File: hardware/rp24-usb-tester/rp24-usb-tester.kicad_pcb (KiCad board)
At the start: 2 copper layers, 50 x 25 mm, 40 parts, among them J1 SPEAKER, J2 POWER, J3 EXT_CAP, J4 505070-2422, J5 RAILS, J6 AUX, J7 MOTOR, P1 USB_C_Receptacle_USB2.0_16P, Q1 SS8050, Q2 SS8050, Q3 SS8050, Q4 SS8050, Q5 SS8050, U1 MT2492

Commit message: chore: include 3d components
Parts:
- C1, C3: footprint Capacitor_SMD:C_0805_2012Metric -> rp24-usb-tester:C_0805_2012Metric
- C2: footprint Capacitor_SMD:C_0402_1005Metric -> rp24-usb-tester:C_0402_1005Metric
- D1, D10, D11, D12, D14, D2, D3, D4, D5, D6, D7, D8, D9: footprint LED_SMD:LED_0603_1608Metric -> rp24-usb-tester:LED_0603_1608Metric
- D13: footprint Diode_SMD:D_SMA -> rp24-usb-tester:D_SMA
- J1, J3, J5, J7: footprint Connector_PinHeader_2.54mm:PinHeader_1x02_P2.54mm_Vertical -> rp24-usb-tester:PinHeader_1x02_P2.54mm_Vertical
- J2: footprint Connector_PinHeader_2.54mm:PinHeader_1x04_P2.54mm_Vertical -> rp24-usb-tester:PinHeader_1x04_P2.54mm_Vertical
- J6: footprint Connector_PinHeader_2.54mm:PinHeader_1x05_P2.54mm_Vertical -> rp24-usb-tester:PinHeader_1x05_P2.54mm_Vertical
- P1: footprint Connector_USB:USB_C_Receptacle_GCT_USB4105-xx-A_16P_TopMnt_Horizontal -> rp24-usb-tester:USB_C_Receptacle_GCT_USB4105-xx-A_16P_TopMnt_Horizontal
- Q1, Q2, Q3, Q4, Q5: footprint Package_TO_SOT_SMD:SOT-23 -> rp24-usb-tester:SOT-23
- R1, R2, R5: footprint Resistor_SMD:R_0402_1005Metric -> rp24-usb-tester:R_0402_1005Metric
- R3, R4: footprint Resistor_SMD:R_0603_1608Metric -> rp24-usb-tester:R_0603_1608Metric
- RN1, RN2, RN3: footprint Resistor_SMD:R_Array_Concave_4x0402 -> rp24-usb-tester:R_Array_Concave_4x0402
- U1: footprint Package_TO_SOT_SMD:SOT-23-6 -> rp24-usb-tester:SOT-23-6

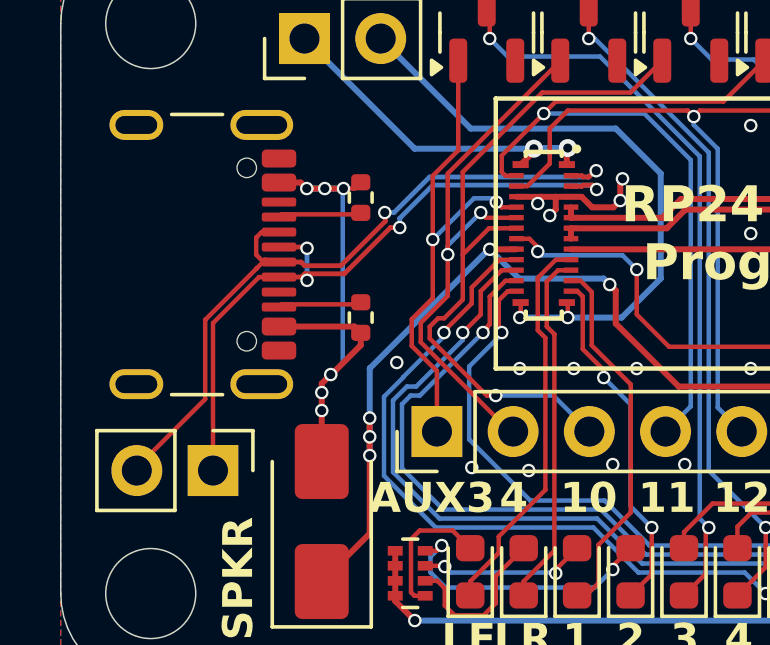
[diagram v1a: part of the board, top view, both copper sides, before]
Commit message: fix: 5.1k resistors go to gnd
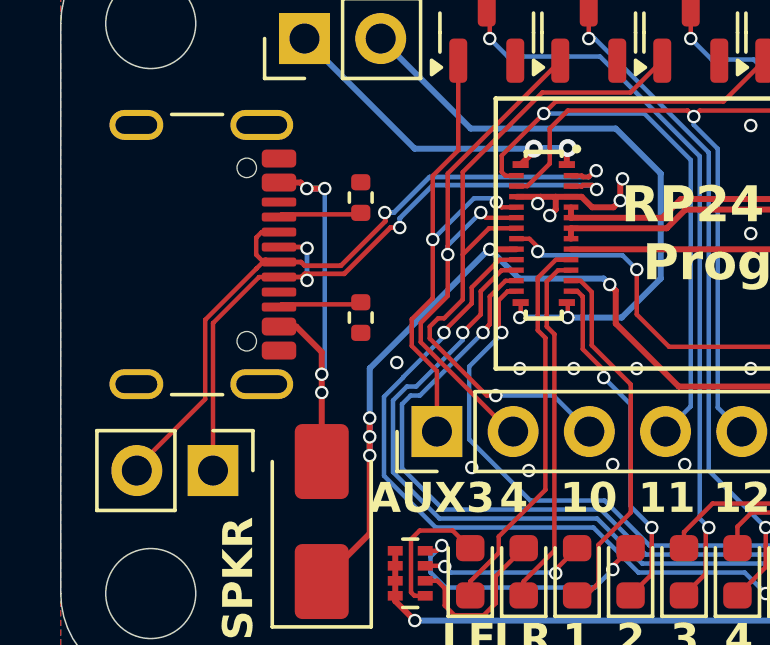
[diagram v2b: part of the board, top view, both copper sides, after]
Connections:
- R1 pad 2: VBUS -> GND
- R2 pad 1: VBUS -> GND
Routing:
- net VBUS: track 19.5 -> 14.5 mm, vias 6 -> 4
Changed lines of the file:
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@@
 			(psa4output no)
 			(plot_black_and_white yes)
-			(plotinvisibletext no)
 			(sketchpadsonfab no)
 			(plotpadnumbers no)
@@
 			)
 		)
-		(property "Datasheet" ""
+		(property "Datasheet" "~"
 			(at 0 0 90)
 			(unlocked yes)
@@
 			)
 		)
-		(property "Datasheet" ""
+		(property "Datasheet" "~"
 			(at 0 0 90)
 			(unlocked yes)
@@
 			)
 		)
-		(property "Datasheet" ""
+		(property "Datasheet" "~"
 			(at 0 0 90)
 			(unlocked yes)
@@
 			)
 		)
-		(property "Datasheet" ""
+		(property "Datasheet" "~"
 			(at 0 0 90)
 			(unlocked yes)
@@
 			)
 		)
-		(property "Datasheet" ""
+		(property "Datasheet" "~"
 			(at 0 0 90)
 			(unlocked yes)
@@
 			)
 		)
-		(property "Datasheet" ""
+		(property "Datasheet" "~"
 			(at 0 0 0)
 			(unlocked yes)
@@
 			)
 		)
-		(property "Datasheet" ""
+		(property "Datasheet" "~"
 			(at 0 0 0)
 			(unlocked yes)
@@
 			)
 		)
-		(property "Datasheet" ""
+		(property "Datasheet" "~"
 			(at 0 0 90)
 			(unlocked yes)
@@
 			)
 		)
-		(property "Datasheet" ""
+		(property "Datasheet" "~"
 			(at 0 0 90)
 			(unlocked yes)
@@
 			)
 		)
-		(property "Datasheet" ""
+		(property "Datasheet" "~"
 			(at 0 0 90)
 			(unlocked yes)
@@
 			(layers "F.Cu" "F.Mask" "F.Paste")
 			(roundrect_rratio 0.25)
-			(net 47 "VBUS")
+			(net 26 "GND")
 			(pintype "passive")
 		)
@@
 			)
 		)
-		(property "Datasheet" ""
+		(property "Datasheet" "~"
 			(at 0 0 90)
 			(unlocked yes)
@@
 			)
 		)
-		(property "Datasheet" ""
+		(property "Datasheet" "~"
 			(at 0 0 90)
 			(unlocked yes)
@@
 			)
 		)
-		(property "Datasheet" ""
+		(property "Datasheet" "~"
 			(at 0 0 90)
 			(unlocked yes)
@@
 			)
 		)
-		(property "Datasheet" ""
+		(property "Datasheet" "~"
 			(at 0 0 0)
 			(unlocked yes)
@@
 			)
 		)
-		(property "Datasheet" ""
+		(property "Datasheet" "~"
 			(at 0 0 90)
 			(unlocked yes)
@@
 			(layers "F.Cu" "F.Mask" "F.Paste")
 			(roundrect_rratio 0.25)
-			(net 47 "VBUS")
+			(net 26 "GND")
 			(pintype "passive")
 		)
@@
 			)
 		)
-		(property "Datasheet" ""
+		(property "Datasheet" "~"
 			(at 0 0 270)
 			(unlocked yes)
@@
 			)
 		)
-		(property "Datasheet" ""
+		(property "Datasheet" "~"
 			(at 0 0 180)
 			(unlocked yes)
@@
 			)
 		)
-		(property "Datasheet" ""
+		(property "Datasheet" "~"
 			(at 0 0 90)
 			(unlocked yes)
@@
 			)
 		)
-		(property "Datasheet" ""
+		(property "Datasheet" "~"
 			(at 0 0 90)
 			(unlocked yes)
@@
 			)
 		)
-		(property "Datasheet" ""
+		(property "Datasheet" "~"
 			(at 0 0 90)
 			(unlocked yes)
@@
 			)
 		)
-		(property "Datasheet" ""
+		(property "Datasheet" "~"
 			(at 0 0 0)
 			(layer "F.Fab")
@@
 			)
 		)
-		(property "Datasheet" ""
+		(property "Datasheet" "~"
 			(at 0 0 90)
 			(unlocked yes)
@@
 			)
 		)
-		(property "Datasheet" ""
+		(property "Datasheet" "~"
 			(at 0 0 90)
 			(unlocked yes)
@@
 			)
 		)
-		(property "Datasheet" ""
+		(property "Datasheet" "~"
 			(at 0 0 90)
 			(unlocked yes)
@@
 			)
 		)
-		(property "Datasheet" ""
+		(property "Datasheet" "~"
 			(at 0 0 270)
 			(unlocked yes)
@@
 			)
 		)
-		(property "Datasheet" ""
+		(property "Datasheet" "~"
 			(at 0 0 270)
 			(unlocked yes)
@@
 			)
 		)
-		(property "Datasheet" ""
+		(property "Datasheet" "~"
 			(at 0 0 90)
 			(unlocked yes)
@@
 			)
 		)
-		(property "Datasheet" ""
+		(property "Datasheet" "~"
 			(at 0 0 0)
 			(unlocked yes)
@@
 			)
 		)
-		(property "Datasheet" ""
+		(property "Datasheet" "~"
 			(at 0 0 90)
 			(unlocked yes)
@@
 			)
 		)
-		(property "Datasheet" ""
+		(property "Datasheet" "~"
 			(at 0 0 90)
 			(unlocked yes)
@@
 			)
 		)
-		(property "Datasheet" ""
+		(property "Datasheet" "~"
 			(at 0 0 90)
 			(unlocked yes)
@@
 	)
 	(segment
-		(start 134.3 108)
-		(end 133.7 108)
+		(start 134.2 113.450001)
+		(end 134.2 114.19)
 		(width 0.2)
 		(layer "F.Cu")
@@
 	)
 	(segment
-		(start 134.925003 108)
-		(end 134.3 108)
+		(start 134.3 108)
+		(end 133.7 108)
 		(width 0.2)
 		(layer "F.Cu")
@@
 	)
 	(segment
-		(start 134.5 114.2)
-		(end 134.525 114.2)
-		(width 0.4)
-		(layer "F.Cu")
-		(net 47)
-	)
-	(segment
-		(start 135.5 113.225)
-		(end 134.525 114.2)
+		(start 132.775 112.6)
+		(end 133.349999 112.6)
 		(width 0.2)
 		(layer "F.Cu")
@@
 	)
 	(segment
-		(start 134.5 114.2)
-		(end 134.2 114.5)
-		(width 0.2)
-		(layer "F.Cu")
-		(net 47)
-	)
-	(segment
 		(start 133.5 107.8)
 		(end 133.7 108)
@@
 	)
 	(segment
-		(start 135.29 112.6)
-		(end 135.5 112.81)
-		(width 0.2)
-		(layer "F.Cu")
-		(net 47)
-	)
-	(segment
-		(start 135.5 112.81)
-		(end 135.5 113.225)
-		(width 0.2)
-		(layer "F.Cu")
-		(net 47)
-	)
-	(segment
-		(start 135.29 108)
-		(end 135.5 107.79)
-		(width 0.15)
-		(layer "F.Cu")
-		(net 47)
-	)
-	(segment
-		(start 134.2 114.5)
+		(start 134.2 114.19)
 		(end 134.2 117.1)
 		(width 0.2)
@@
 	)
 	(segment
-		(start 134.925003 108)
-		(end 135.29 108)
-		(width 0.15)
+		(start 133.349999 112.6)
+		(end 134.2 113.450001)
+		(width 0.2)
 		(layer "F.Cu")
 		(net 47)
 	)
 	(segment
-		(start 132.775 112.6)
-		(end 135.29 112.6)
-		(width 0.2)
+		(start 134.2 114.19)
+		(end 134.21 114.2)
+		(width 0.4)
 		(layer "F.Cu")
 		(net 47)
 	)
 	(via
-		(at 134.5 114.2)
-		(size 0.45)
-		(drill 0.3)
-		(layers "F.Cu" "B.Cu")
-		(net 47)
-	)
-	(via
-		(at 134.2 115.4)
+		(at 134.2 114.19)
 		(size 0.45)
 		(drill 0.3)
@@
 		(net 47)
 	)
-	(via
-		(at 134.925003 108)
-		(size 0.45)
-		(drill 0.3)
-		(layers "F.Cu" "B.Cu")
-		(net 47)
-	)
 	(segment
 		(start 133.7 108)
-		(end 134.925003 108)
+		(end 134.3 108)
 		(width 0.2)
 		(layer "B.Cu")
@@
 	)
 	(segment
-		(start 134.2 114.5)
-		(end 134.5 114.2)
-		(width 0.15)
-		(layer "B.Cu")
-		(net 47)
-	)
-	(segment
-		(start 134.5 114.2)
-		(end 134.9 113.8)
-		(width 0.15)
-		(layer "B.Cu")
-		(net 47)
-	)
-	(segment
-		(start 134.2 115.4)
-		(end 134.2 114.5)
+		(start 134.2 114.19)
+		(end 134.2 114.8)
 		(width 0.15)
 		(layer "B.Cu")
@@
 	)
 	(segment
-		(start 134.9 113.8)
-		(end 134.9 108.025003)
+		(start 134.3 108)
+		(end 134.3 114.09)
 		(width 0.15)
 		(layer "B.Cu")
@@
 	)
 	(segment
-		(start 134.9 108.025003)
-		(end 134.925003 108)
+		(start 134.3 114.09)
+		(end 134.2 114.19)
 		(width 0.15)
 		(layer "B.Cu")
